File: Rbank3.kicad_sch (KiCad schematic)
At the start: 118 parts, among them K33 TQ2-5, K34 TQ2-5, K35 TQ2-5, K36 TQ2-5, K37 TQ2-5, K38 TQ2-5, K39 TQ2-5, K40 TQ2-5, K41 TQ2-5, Q46 2N2222, Q47 2N2222, Q48 2N2222, Q49 2N2222, Q50 2N2222, Q51 2N2222, Q52 2N2222, Q53 2N2222, Q54 2N2222

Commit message: First try to fit electronic on PCB
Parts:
- removed D69, D70, D71, D72, D77, D78, D79, D80, D85: LED, LED_THT:LED_D3.0mm_Clear, symbol Device:LED
- removed R115, R116, R117, R118, R123, R124, R125, R126, R131: 220, Resistor_THT:R_Axial_DIN0309_L9.0mm_D3.2mm_P12.70mm_Horizontal, symbol Device:R_US
- TP118: renamed from TP233; footprint Connector_Pin:Pin_D1.2mm_L11.3mm_W3.0mm_Flat -> Connector_Pin:Pin_D1.0mm_L10.0mm
- TP119: renamed from TP234; footprint Connector_Pin:Pin_D1.2mm_L11.3mm_W3.0mm_Flat -> Connector_Pin:Pin_D1.0mm_L10.0mm
- TP120: renamed from TP235; footprint Connector_Pin:Pin_D1.2mm_L11.3mm_W3.0mm_Flat -> Connector_Pin:Pin_D1.0mm_L10.0mm
- TP121: renamed from TP236; footprint Connector_Pin:Pin_D1.2mm_L11.3mm_W3.0mm_Flat -> Connector_Pin:Pin_D1.0mm_L10.0mm
- TP122: renamed from TP237; footprint Connector_Pin:Pin_D1.2mm_L11.3mm_W3.0mm_Flat -> Connector_Pin:Pin_D1.0mm_L10.0mm
- TP123: renamed from TP238; footprint Connector_Pin:Pin_D1.2mm_L11.3mm_W3.0mm_Flat -> Connector_Pin:Pin_D1.0mm_L10.0mm
- TP124: renamed from TP239; footprint Connector_Pin:Pin_D1.2mm_L11.3mm_W3.0mm_Flat -> Connector_Pin:Pin_D1.0mm_L10.0mm
- TP125: renamed from TP240; footprint Connector_Pin:Pin_D1.2mm_L11.3mm_W3.0mm_Flat -> Connector_Pin:Pin_D1.0mm_L10.0mm
- TP126: renamed from TP241; footprint Connector_Pin:Pin_D1.2mm_L11.3mm_W3.0mm_Flat -> Connector_Pin:Pin_D1.0mm_L10.0mm
- TP127: renamed from TP242; footprint Connector_Pin:Pin_D1.2mm_L11.3mm_W3.0mm_Flat -> Connector_Pin:Pin_D1.0mm_L10.0mm
- TP128: renamed from TP243; footprint Connector_Pin:Pin_D1.2mm_L11.3mm_W3.0mm_Flat -> Connector_Pin:Pin_D1.0mm_L10.0mm
- TP129: renamed from TP244; footprint Connector_Pin:Pin_D1.2mm_L11.3mm_W3.0mm_Flat -> Connector_Pin:Pin_D1.0mm_L10.0mm
- TP130: renamed from TP245; footprint Connector_Pin:Pin_D1.2mm_L11.3mm_W3.0mm_Flat -> Connector_Pin:Pin_D1.0mm_L10.0mm
- TP131: renamed from TP246; footprint Connector_Pin:Pin_D1.2mm_L11.3mm_W3.0mm_Flat -> Connector_Pin:Pin_D1.0mm_L10.0mm
- TP132: renamed from TP247; footprint Connector_Pin:Pin_D1.2mm_L11.3mm_W3.0mm_Flat -> Connector_Pin:Pin_D1.0mm_L10.0mm
- TP133: renamed from TP248; footprint Connector_Pin:Pin_D1.2mm_L11.3mm_W3.0mm_Flat -> Connector_Pin:Pin_D1.0mm_L10.0mm
- renumbered D73 to D46, D74 to D47, D75 to D48, D76 to D49, D81 to D50, D82 to D51, D83 to D52, D84 to D53, D86 to D54, NT527 to NT541, NT528 to NT542, NT529 to NT543, NT530 to NT544, NT531 to NT545, NT532 to NT546, NT533 to NT547, NT534 to NT548, NT535 to NT549, NT536 to NT550, NT537 to NT551, NT538 to NT552, NT539 to NT553, NT540 to NT554, NT541 to NT555, NT542 to NT556, NT543 to NT557, NT544 to NT558, NT545 to NT559, NT546 to NT560, NT547 to NT561, NT548 to NT562, NT549 to NT563, NT550 to NT564, NT551 to NT565, NT552 to NT566, NT553 to NT567, NT554 to NT568, NT555 to NT569, NT556 to NT570, NT557 to NT571, NT558 to NT572, NT559 to NT573, NT560 to NT574, NT561 to NT575, NT562 to NT576, NT563 to NT577, NT564 to NT578, NT565 to NT579, NT566 to NT580, NT567 to NT581, NT568 to NT582, NT569 to NT583, NT570 to NT584, NT571 to NT585, NT572 to NT586, NT573 to NT587, Q46 to Q49, Q47 to Q50, Q48 to Q51, Q49 to Q52, Q50 to Q53, Q51 to Q54, Q52 to Q55, Q53 to Q56, Q54 to Q57, R130 to R100, R132 to R101, R119 to R93, R120 to R94, R121 to R95, R122 to R96, R127 to R97, R128 to R98, R129 to R99

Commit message: backup 1 bank done
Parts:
- removed D46, D47, D48, D49, D50, D51, D52, D53, D54: 1N4148, Diode_THT:D_DO-35_SOD27_P7.62mm_Horizontal, symbol Diode:1N4148
- removed NT541: NT30_H, NetTie:NetTie-2_THT_Pad1.0mm, symbol Device:NetTie_2
- removed NT542: NT31_H, NetTie:NetTie-2_THT_Pad1.0mm, symbol Device:NetTie_2
- removed NT543: NT32_H, NetTie:NetTie-2_THT_Pad1.0mm, symbol Device:NetTie_2
- removed NT544: NT33_H, NetTie:NetTie-2_THT_Pad1.0mm, symbol Device:NetTie_2
- removed NT545: NT30_CH, NetTie:NetTie-2_THT_Pad1.0mm, symbol Device:NetTie_2
- removed NT546: NT31_CH, NetTie:NetTie-2_THT_Pad1.0mm, symbol Device:NetTie_2
- removed NT547: NT32_CH, NetTie:NetTie-2_THT_Pad1.0mm, symbol Device:NetTie_2
- removed NT548: NT33_CH, NetTie:NetTie-2_THT_Pad1.0mm, symbol Device:NetTie_2
- removed NT549: NT30_L, NetTie:NetTie-2_THT_Pad1.0mm, symbol Device:NetTie_2
- removed NT550: NT31_L, NetTie:NetTie-2_THT_Pad1.0mm, symbol Device:NetTie_2
- removed NT551: NT32_L, NetTie:NetTie-2_THT_Pad1.0mm, symbol Device:NetTie_2
- removed NT552: NT33_L, NetTie:NetTie-2_THT_Pad1.0mm, symbol Device:NetTie_2
- removed NT553: NT30_CL, NetTie:NetTie-2_THT_Pad1.0mm, symbol Device:NetTie_2
- removed NT554: NT31_CL, NetTie:NetTie-2_THT_Pad1.0mm, symbol Device:NetTie_2
- removed NT555: NT32_CL, NetTie:NetTie-2_THT_Pad1.0mm, symbol Device:NetTie_2
- removed NT556: NT33_CL, NetTie:NetTie-2_THT_Pad1.0mm, symbol Device:NetTie_2
- removed NT557: NT30_D, NetTie:NetTie-2_THT_Pad1.0mm, symbol Device:NetTie_2
- removed NT558: NT31_D, NetTie:NetTie-2_THT_Pad1.0mm, symbol Device:NetTie_2
- removed NT559: NT32_D, NetTie:NetTie-2_THT_Pad1.0mm, symbol Device:NetTie_2
- removed NT560: NT33_D, NetTie:NetTie-2_THT_Pad1.0mm, symbol Device:NetTie_2
- removed NT561: NT34_H, NetTie:NetTie-2_THT_Pad1.0mm, symbol Device:NetTie_2
- removed NT562: NT35_H, NetTie:NetTie-2_THT_Pad1.0mm, symbol Device:NetTie_2
- removed NT563: NT36_H, NetTie:NetTie-2_THT_Pad1.0mm, symbol Device:NetTie_2
- removed NT564: NT37_H, NetTie:NetTie-2_THT_Pad1.0mm, symbol Device:NetTie_2
- removed NT565: NT34_CH, NetTie:NetTie-2_THT_Pad1.0mm, symbol Device:NetTie_2
- removed NT566: NT35_CH, NetTie:NetTie-2_THT_Pad1.0mm, symbol Device:NetTie_2
- removed NT567: NT36_CH, NetTie:NetTie-2_THT_Pad1.0mm, symbol Device:NetTie_2
- removed NT568: NT37_CH, NetTie:NetTie-2_THT_Pad1.0mm, symbol Device:NetTie_2
- removed NT569: NT34_L, NetTie:NetTie-2_THT_Pad1.0mm, symbol Device:NetTie_2
- removed NT570: NT35_L, NetTie:NetTie-2_THT_Pad1.0mm, symbol Device:NetTie_2
- removed NT571: NT36_L, NetTie:NetTie-2_THT_Pad1.0mm, symbol Device:NetTie_2
- removed NT572: NT37_L, NetTie:NetTie-2_THT_Pad1.0mm, symbol Device:NetTie_2
- removed NT573: NT34_CL, NetTie:NetTie-2_THT_Pad1.0mm, symbol Device:NetTie_2
- removed NT574: NT35_CL, NetTie:NetTie-2_THT_Pad1.0mm, symbol Device:NetTie_2
- removed NT575: NT36_CL, NetTie:NetTie-2_THT_Pad1.0mm, symbol Device:NetTie_2
- removed NT576: NT37_CL, NetTie:NetTie-2_THT_Pad1.0mm, symbol Device:NetTie_2
- removed NT577: NT34_D, NetTie:NetTie-2_THT_Pad1.0mm, symbol Device:NetTie_2
- removed NT578: NT35_D, NetTie:NetTie-2_THT_Pad1.0mm, symbol Device:NetTie_2
- removed NT579: NT36_D, NetTie:NetTie-2_THT_Pad1.0mm, symbol Device:NetTie_2
- removed NT580: NT37_D, NetTie:NetTie-2_THT_Pad1.0mm, symbol Device:NetTie_2
- removed NT581, NT584: NT3S_RL, NetTie:NetTie-2_THT_Pad1.0mm, symbol Device:NetTie_2
- removed NT582: NT3S_CH, NetTie:NetTie-2_THT_Pad1.0mm, symbol Device:NetTie_2
- removed NT583: NT3S_NH, NetTie:NetTie-2_THT_Pad1.0mm, symbol Device:NetTie_2
- removed NT585: NT3S_CL, NetTie:NetTie-2_THT_Pad1.0mm, symbol Device:NetTie_2
- removed NT586: NT3S_L1, NetTie:NetTie-2_THT_Pad1.0mm, symbol Device:NetTie_2
- removed NT587: NT3S_D, NetTie:NetTie-2_THT_Pad1.0mm, symbol Device:NetTie_2
- removed Q49, Q50, Q51, Q52, Q53, Q54, Q55, Q56, Q57: 2N2222, Package_TO_SOT_THT:TO-92_Inline, symbol Transistor_BJT:2N3904
- removed R100, R101, R93, R94, R95, R96, R97, R98, R99: 10K, Resistor_THT:R_Axial_DIN0309_L9.0mm_D3.2mm_P12.70mm_Horizontal, symbol Device:R_US
- removed TP127: NT35_HH, Connector_Pin:Pin_D1.0mm_L10.0mm, symbol Connector:TestPoint
- removed TP128: NT36_HH, Connector_Pin:Pin_D1.0mm_L10.0mm, symbol Connector:TestPoint
- removed TP129: NT37_HH, Connector_Pin:Pin_D1.0mm_L10.0mm, symbol Connector:TestPoint
- removed TP130: NT34_LL, Connector_Pin:Pin_D1.0mm_L10.0mm, symbol Connector:TestPoint
- removed TP131: NT35_LL, Connector_Pin:Pin_D1.0mm_L10.0mm, symbol Connector:TestPoint
- removed TP132: NT36_LL, Connector_Pin:Pin_D1.0mm_L10.0mm, symbol Connector:TestPoint
- removed TP133: NT37_LL, Connector_Pin:Pin_D1.0mm_L10.0mm, symbol Connector:TestPoint
- added NT368: NT30_CH, NetTie:NetTie-2_Front1.0mm, symbol Device:NetTie_2
- added NT369: NT31_CH, NetTie:NetTie-2_Front1.0mm, symbol Device:NetTie_2
- added NT370: NT32_CH, NetTie:NetTie-2_Front1.0mm, symbol Device:NetTie_2
- added NT371: NT33_CH, NetTie:NetTie-2_Front1.0mm, symbol Device:NetTie_2
- added NT372: NT30_CL, NetTie:NetTie-2_Front1.0mm, symbol Device:NetTie_2
- added NT373: NT31_CL, NetTie:NetTie-2_Front1.0mm, symbol Device:NetTie_2
- added NT374: NT32_CL, NetTie:NetTie-2_Front1.0mm, symbol Device:NetTie_2
- added NT375: NT33_CL, NetTie:NetTie-2_Front1.0mm, symbol Device:NetTie_2
- added NT376: NT34_CH, NetTie:NetTie-2_Front1.0mm, symbol Device:NetTie_2
- added NT377: NT35_CH, NetTie:NetTie-2_Front1.0mm, symbol Device:NetTie_2
- added NT378: NT36_CH, NetTie:NetTie-2_Front1.0mm, symbol Device:NetTie_2
- added NT379: NT37_CH, NetTie:NetTie-2_Front1.0mm, symbol Device:NetTie_2
- added NT380: NT34_CL, NetTie:NetTie-2_Front1.0mm, symbol Device:NetTie_2
- added NT381: NT35_CL, NetTie:NetTie-2_Front1.0mm, symbol Device:NetTie_2
- added NT382: NT36_CL, NetTie:NetTie-2_Front1.0mm, symbol Device:NetTie_2
- added NT383: NT37_CL, NetTie:NetTie-2_Front1.0mm, symbol Device:NetTie_2
- added NT384, NT387: NT3S_RL, NetTie:NetTie-2_Front1.0mm, symbol Device:NetTie_2
- added NT385: NT3S_CH, NetTie:NetTie-2_Front1.0mm, symbol Device:NetTie_2
- added NT386: NT3S_NH, NetTie:NetTie-2_Front1.0mm, symbol Device:NetTie_2
- added NT388: NT3S_CL, NetTie:NetTie-2_Front1.0mm, symbol Device:NetTie_2
- added NT389: NT3S_L1, NetTie:NetTie-2_Front1.0mm, symbol Device:NetTie_2
- added TP111: NT30_HH, Connector_Pin:Pin_D0.9mm_L10.0mm_W2.4mm_FlatFork, symbol Connector:TestPoint
- added TP112: NT31_HH, Connector_Pin:Pin_D0.9mm_L10.0mm_W2.4mm_FlatFork, symbol Connector:TestPoint
- added TP113: NT32_HH, Connector_Pin:Pin_D0.9mm_L10.0mm_W2.4mm_FlatFork, symbol Connector:TestPoint
- added TP114: NT33_HH, Connector_Pin:Pin_D0.9mm_L10.0mm_W2.4mm_FlatFork, symbol Connector:TestPoint
- added TP115: NT30_LL, Connector_Pin:Pin_D0.9mm_L10.0mm_W2.4mm_FlatFork, symbol Connector:TestPoint
- added TP116: NT31_LL, Connector_Pin:Pin_D0.9mm_L10.0mm_W2.4mm_FlatFork, symbol Connector:TestPoint
- added TP117: NT32_LL, Connector_Pin:Pin_D0.9mm_L10.0mm_W2.4mm_FlatFork, symbol Connector:TestPoint
- TP118: value NT30_HH -> NT33_LL; footprint Connector_Pin:Pin_D1.0mm_L10.0mm -> Connector_Pin:Pin_D0.9mm_L10.0mm_W2.4mm_FlatFork
- TP119: value NT31_HH -> NT34_HH; footprint Connector_Pin:Pin_D1.0mm_L10.0mm -> Connector_Pin:Pin_D0.9mm_L10.0mm_W2.4mm_FlatFork
- TP120: value NT32_HH -> NT35_HH; footprint Connector_Pin:Pin_D1.0mm_L10.0mm -> Connector_Pin:Pin_D0.9mm_L10.0mm_W2.4mm_FlatFork
- TP121: value NT33_HH -> NT36_HH; footprint Connector_Pin:Pin_D1.0mm_L10.0mm -> Connector_Pin:Pin_D0.9mm_L10.0mm_W2.4mm_FlatFork
- TP122: value NT30_LL -> NT37_HH; footprint Connector_Pin:Pin_D1.0mm_L10.0mm -> Connector_Pin:Pin_D0.9mm_L10.0mm_W2.4mm_FlatFork
- TP123: value NT31_LL -> NT34_LL; footprint Connector_Pin:Pin_D1.0mm_L10.0mm -> Connector_Pin:Pin_D0.9mm_L10.0mm_W2.4mm_FlatFork
- TP124: value NT32_LL -> NT35_LL; footprint Connector_Pin:Pin_D1.0mm_L10.0mm -> Connector_Pin:Pin_D0.9mm_L10.0mm_W2.4mm_FlatFork
- TP125: value NT33_LL -> NT36_LL; footprint Connector_Pin:Pin_D1.0mm_L10.0mm -> Connector_Pin:Pin_D0.9mm_L10.0mm_W2.4mm_FlatFork
- TP126: value NT34_HH -> NT37_LL; footprint Connector_Pin:Pin_D1.0mm_L10.0mm -> Connector_Pin:Pin_D0.9mm_L10.0mm_W2.4mm_FlatFork
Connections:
- net B30_CH: now also NT368.2
- net B30_CL: now also NT372.2
- net B30_H: now also K33.7
- net B30_L: now also K33.4
- net B31_CH: now also NT369.2
- net B31_CL: now also NT373.2
- net B31_H: now also K34.7
- net B31_L: now also K34.4
- net B32_CH: now also NT370.2
- net B32_CL: now also NT374.2
- net B32_H: now also K35.7
- net B32_L: now also K35.4
- net B33_CH: now also NT371.2
- net B33_CL: now also NT375.2
- net B33_H: now also K36.7
- net B33_L: now also K36.4
- net B34_CH: now also NT376.2
- net B34_CL: now also NT380.2
- net B34_H: now also K37.7
- net B34_L: now also K37.4
- net B35_CH: now also NT377.2
- net B35_CL: now also NT381.2
- net B35_H: now also K38.7
- net B35_L: now also K38.4
- net B36_CH: now also NT378.2
- net B36_CL: now also NT382.2
- net B36_H: now also K39.7
- net B36_L: now also K39.4
- net B37_CH: now also NT379.2
- net B37_CL: now also NT383.2
- net B37_H: now also K40.7
- net B37_L: now also K40.4
- net B3_COM_H: now also NT385.1
- net B3_COM_L: now also NT388.1
- net BANK3_BUS_H: now also NT372.1, NT373.1, NT374.1, NT375.1, NT380.1, NT381.1, NT382.1, NT383.1, NT386.2, NT387.2
- net BANK3_BUS_L: now also NT368.1, NT369.1, NT370.1, NT371.1, NT376.1, NT377.1, NT378.1, NT379.1, NT384.2, NT389.2
- net at TP124.1: now also K38.2; no longer K35.2
- net B30_R: now reaches K33.10
- net at TP122.1: now also K40.9; no longer K33.2
- net at K33.9: now also TP111.1; no longer TP118.1
- net B33_R: now reaches K36.10
- net at K41.9: now also NT386.1
- net at K41.8: now also NT385.2
- net at K40.2: now also TP126.1
- net at K34.2: now also TP116.1; no longer TP123.1
- net at K34.9: now also TP112.1; no longer TP119.1
- net at K39.9: now also TP121.1
- net at K41.7: now also NT384.1
- net at K37.9: now also TP119.1; no longer TP126.1
- net B36_R: now reaches K39.10
- net at K39.2: now also TP125.1
- net B34_R: now reaches K37.10
- net B37_R: now reaches K40.10
- net at K36.2: now also TP118.1; no longer TP125.1
- net at K36.9: now also TP114.1; no longer TP121.1
- net at K38.9: now also TP120.1
- net B35_R: now reaches K38.10
- net at K37.2: now also TP123.1
- net at K35.9: now also TP113.1; no longer TP120.1
- net B3S_R: now reaches K41.10
- net at K41.2: now also NT389.1
- net B32_R: now reaches K35.10
- net at K41.4: now also NT387.1
- net at K41.3: now also NT388.2
- new net: K35.2, TP117.1
- new net: K33.2, TP115.1

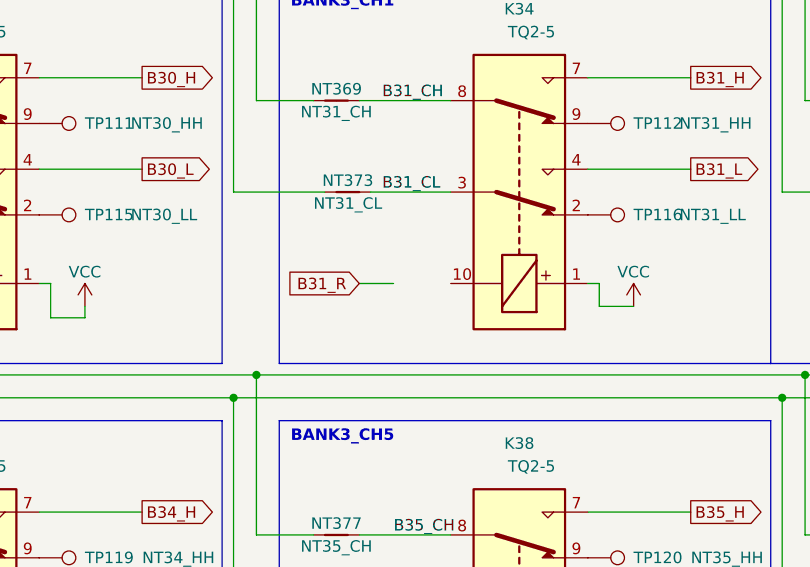
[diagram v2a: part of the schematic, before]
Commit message: half PCB completed
FTS io controller PCB
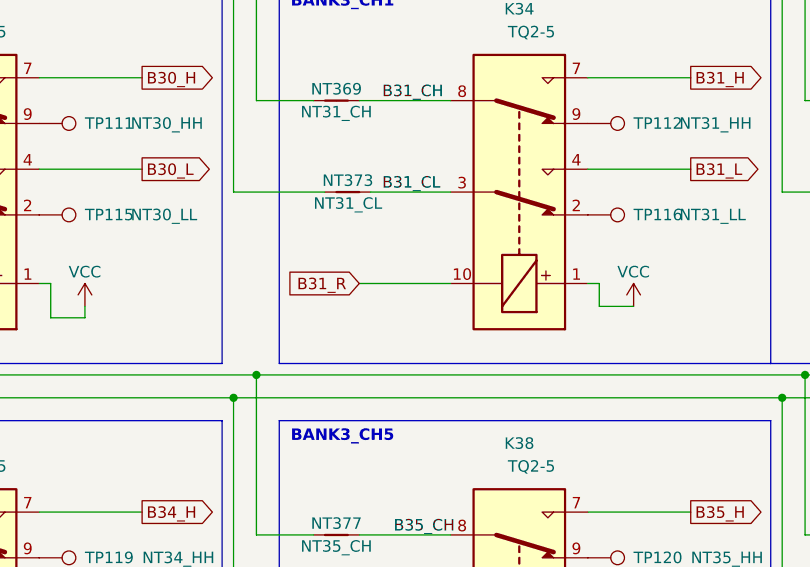
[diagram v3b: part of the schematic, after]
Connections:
- net B31_R: now also K34.10
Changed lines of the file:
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@@
-    (stroke (width 0) (type default) (color 0 0 0 0))
-  )
-  (wire (pts (xy 90.17 50.8) (xy 93.98 50.8))
     (stroke (width 0) (type default) (color 0 0 0 0))
   )
@@
     (stroke (width 0) (type default) (color 0 0 0 0))
   )
+  (wire (pts (xy 90.17 50.8) (xy 100.33 50.8))
+    (stroke (width 0) (type default) (color 0 0 0 0))
+  )

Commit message: PCB Completed
PCB completed but final verification not completed
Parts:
- TP111, TP112, TP113, TP114, TP115, TP116, TP117, TP118, TP119, TP120, TP121, TP122, TP123, TP124, TP125, TP126: footprint Connector_Pin:Pin_D0.9mm_L10.0mm_W2.4mm_FlatFork -> TestPoint:TestPoint_THTPad_D1.5mm_Drill0.7mm
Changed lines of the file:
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@@
       (effects (font (size 1.27 1.27)) (justify left))
     )
-    (property "Footprint" "Connector_Pin:Pin_D0.9mm_L10.0mm_W2.4mm_FlatFork" (id 2) (at 237.49 96.52 0)
+    (property "Footprint" "TestPoint:TestPoint_THTPad_D1.5mm_Drill0.7mm" (id 2) (at 237.49 96.52 0)
       (effects (font (size 1.27 1.27)) hide)
     )
@@
       (effects (font (size 1.27 1.27)) (justify left))
     )
-    (property "Footprint" "Connector_Pin:Pin_D0.9mm_L10.0mm_W2.4mm_FlatFork" (id 2) (at 176.53 86.36 0)
+    (property "Footprint" "TestPoint:TestPoint_THTPad_D1.5mm_Drill0.7mm" (id 2) (at 176.53 86.36 0)
       (effects (font (size 1.27 1.27)) hide)
     )
@@
       (effects (font (size 1.27 1.27)) (justify left))
     )
-    (property "Footprint" "Connector_Pin:Pin_D0.9mm_L10.0mm_W2.4mm_FlatFork" (id 2) (at 176.53 38.1 0)
+    (property "Footprint" "TestPoint:TestPoint_THTPad_D1.5mm_Drill0.7mm" (id 2) (at 176.53 38.1 0)
       (effects (font (size 1.27 1.27)) hide)
     )
@@
       (effects (font (size 1.27 1.27)) (justify left))
     )
-    (property "Footprint" "Connector_Pin:Pin_D0.9mm_L10.0mm_W2.4mm_FlatFork" (id 2) (at 115.57 96.52 0)
+    (property "Footprint" "TestPoint:TestPoint_THTPad_D1.5mm_Drill0.7mm" (id 2) (at 115.57 96.52 0)
       (effects (font (size 1.27 1.27)) hide)
     )
@@
       (effects (font (size 1.27 1.27)) (justify left))
     )
-    (property "Footprint" "Connector_Pin:Pin_D0.9mm_L10.0mm_W2.4mm_FlatFork" (id 2) (at 115.57 86.36 0)
+    (property "Footprint" "TestPoint:TestPoint_THTPad_D1.5mm_Drill0.7mm" (id 2) (at 115.57 86.36 0)
       (effects (font (size 1.27 1.27)) hide)
     )
@@
       (effects (font (size 1.27 1.27)) (justify left))
     )
-    (property "Footprint" "Connector_Pin:Pin_D0.9mm_L10.0mm_W2.4mm_FlatFork" (id 2) (at 54.61 38.1 0)
+    (property "Footprint" "TestPoint:TestPoint_THTPad_D1.5mm_Drill0.7mm" (id 2) (at 54.61 38.1 0)
       (effects (font (size 1.27 1.27)) hide)
     )
@@
       (effects (font (size 1.27 1.27)) (justify left))
     )
-    (property "Footprint" "Connector_Pin:Pin_D0.9mm_L10.0mm_W2.4mm_FlatFork" (id 2) (at 237.49 86.36 0)
+    (property "Footprint" "TestPoint:TestPoint_THTPad_D1.5mm_Drill0.7mm" (id 2) (at 237.49 86.36 0)
       (effects (font (size 1.27 1.27)) hide)
     )
@@
       (effects (font (size 1.27 1.27)) (justify left))
     )
-    (property "Footprint" "Connector_Pin:Pin_D0.9mm_L10.0mm_W2.4mm_FlatFork" (id 2) (at 54.61 48.26 0)
+    (property "Footprint" "TestPoint:TestPoint_THTPad_D1.5mm_Drill0.7mm" (id 2) (at 54.61 48.26 0)
       (effects (font (size 1.27 1.27)) hide)
     )
@@
       (effects (font (size 1.27 1.27)) (justify left))
     )
-    (property "Footprint" "Connector_Pin:Pin_D0.9mm_L10.0mm_W2.4mm_FlatFork" (id 2) (at 54.61 96.52 0)
+    (property "Footprint" "TestPoint:TestPoint_THTPad_D1.5mm_Drill0.7mm" (id 2) (at 54.61 96.52 0)
       (effects (font (size 1.27 1.27)) hide)
     )
@@
       (effects (font (size 1.27 1.27)) (justify left))
     )
-    (property "Footprint" "Connector_Pin:Pin_D0.9mm_L10.0mm_W2.4mm_FlatFork" (id 2) (at 237.49 38.1 0)
+    (property "Footprint" "TestPoint:TestPoint_THTPad_D1.5mm_Drill0.7mm" (id 2) (at 237.49 38.1 0)
       (effects (font (size 1.27 1.27)) hide)
     )
@@
       (effects (font (size 1.27 1.27)) (justify left))
     )
-    (property "Footprint" "Connector_Pin:Pin_D0.9mm_L10.0mm_W2.4mm_FlatFork" (id 2) (at 176.53 48.26 0)
+    (property "Footprint" "TestPoint:TestPoint_THTPad_D1.5mm_Drill0.7mm" (id 2) (at 176.53 48.26 0)
       (effects (font (size 1.27 1.27)) hide)
     )
@@
       (effects (font (size 1.27 1.27)) (justify left))
     )
-    (property "Footprint" "Connector_Pin:Pin_D0.9mm_L10.0mm_W2.4mm_FlatFork" (id 2) (at 115.57 38.1 0)
+    (property "Footprint" "TestPoint:TestPoint_THTPad_D1.5mm_Drill0.7mm" (id 2) (at 115.57 38.1 0)
       (effects (font (size 1.27 1.27)) hide)
     )
@@
       (effects (font (size 1.27 1.27)) (justify left))
     )
-    (property "Footprint" "Connector_Pin:Pin_D0.9mm_L10.0mm_W2.4mm_FlatFork" (id 2) (at 176.53 96.52 0)
+    (property "Footprint" "TestPoint:TestPoint_THTPad_D1.5mm_Drill0.7mm" (id 2) (at 176.53 96.52 0)
       (effects (font (size 1.27 1.27)) hide)
     )
@@
       (effects (font (size 1.27 1.27)) (justify left))
     )
-    (property "Footprint" "Connector_Pin:Pin_D0.9mm_L10.0mm_W2.4mm_FlatFork" (id 2) (at 54.61 86.36 0)
+    (property "Footprint" "TestPoint:TestPoint_THTPad_D1.5mm_Drill0.7mm" (id 2) (at 54.61 86.36 0)
       (effects (font (size 1.27 1.27)) hide)
     )
@@
       (effects (font (size 1.27 1.27)) (justify left))
     )
-    (property "Footprint" "Connector_Pin:Pin_D0.9mm_L10.0mm_W2.4mm_FlatFork" (id 2) (at 115.57 48.26 0)
+    (property "Footprint" "TestPoint:TestPoint_THTPad_D1.5mm_Drill0.7mm" (id 2) (at 115.57 48.26 0)
       (effects (font (size 1.27 1.27)) hide)
     )
@@
       (effects (font (size 1.27 1.27)) (justify left))
     )
-    (property "Footprint" "Connector_Pin:Pin_D0.9mm_L10.0mm_W2.4mm_FlatFork" (id 2) (at 237.49 48.26 0)
-      (effects (font (size 1.27 1.27)) hide)
-    )
+    (property "Footprint" "TestPoint:TestPoint_THTPad_D1.5mm_Drill0.7mm" (id 2) (at 237.49 48.26 0)
+      (effects (font (size 1.27 1.27)) hide)
+    )
